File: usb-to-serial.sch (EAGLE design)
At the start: 3 parts, among them IC1 SX1308, J1 C10418, U1 CH340ESMD

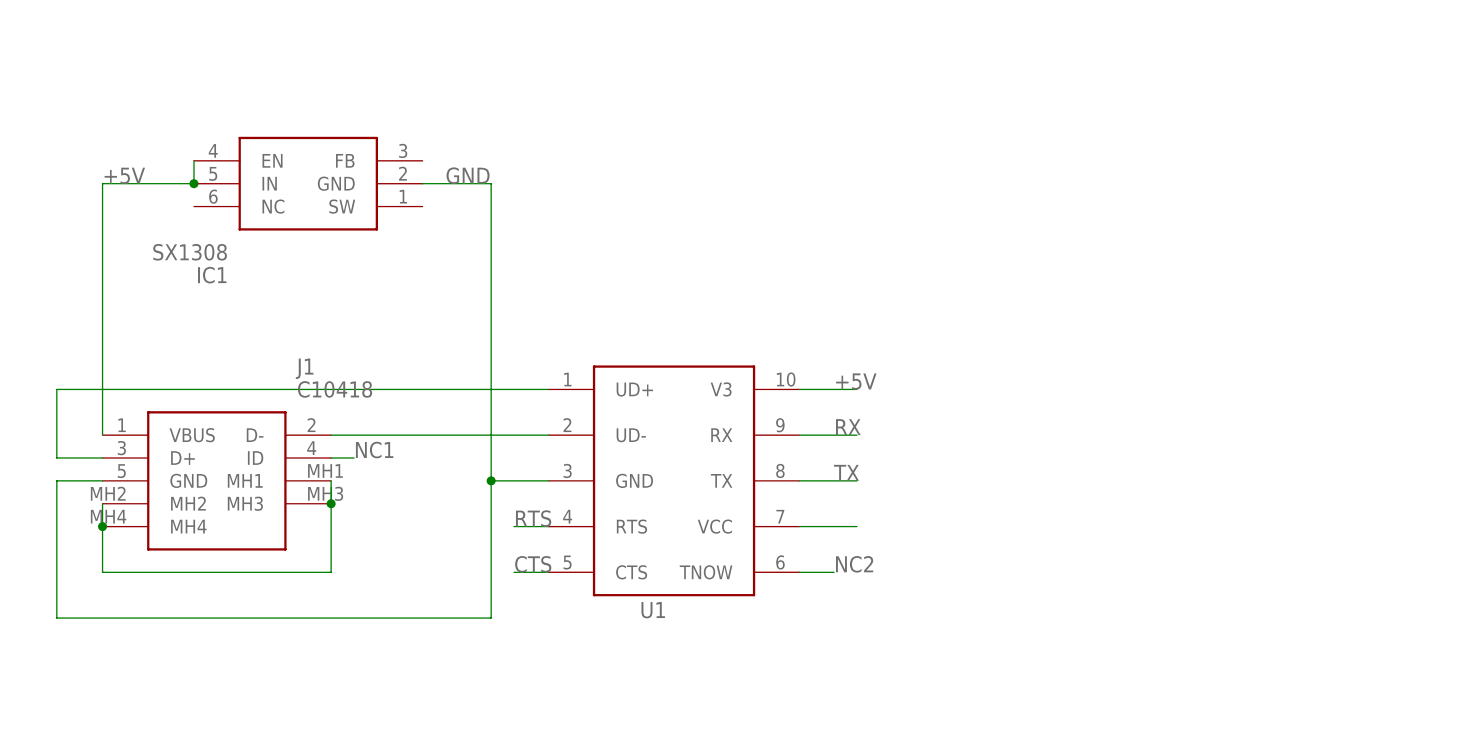
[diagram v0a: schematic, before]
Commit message: USB to Serial done
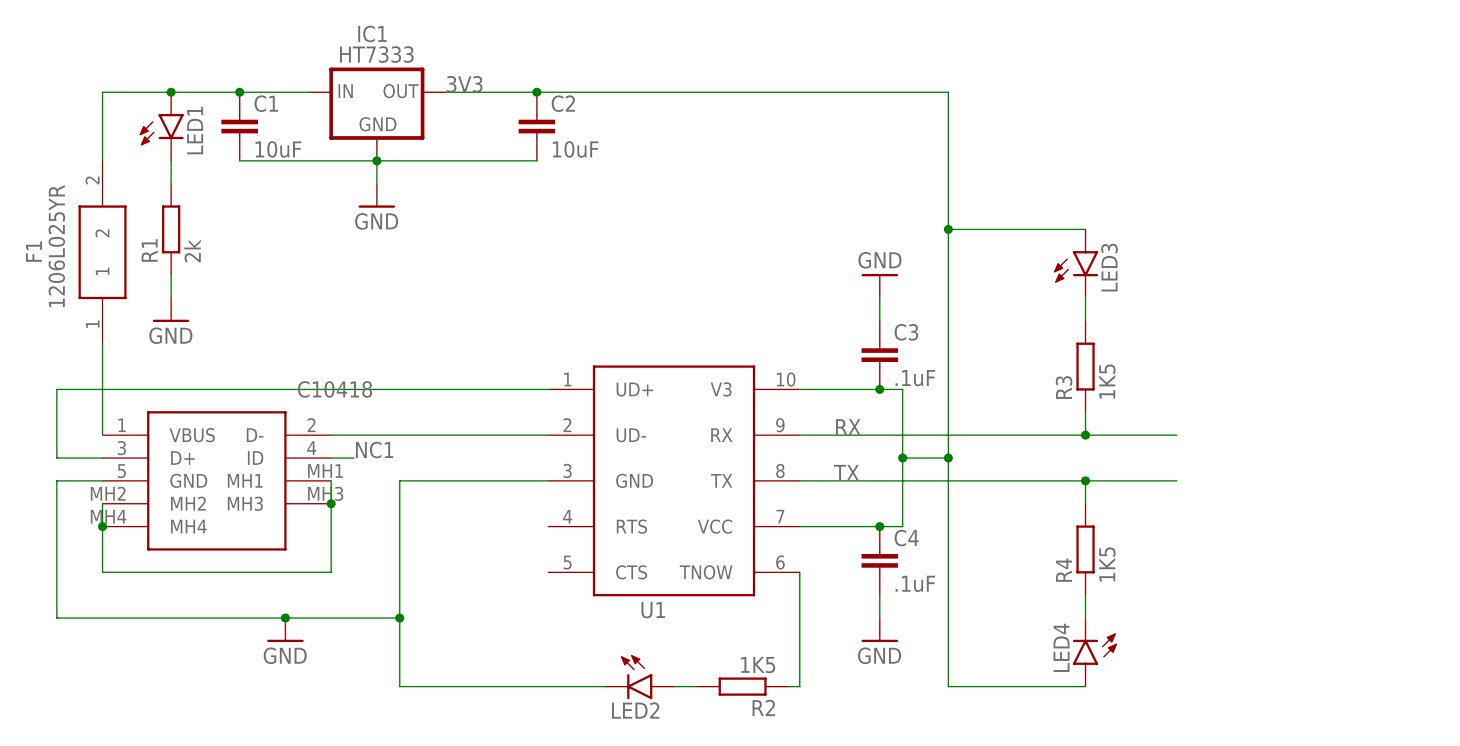
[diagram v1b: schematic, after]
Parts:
- added C1, C2: 10uF, rcl:C-EUC0805
- added C3, C4: .1uF, rcl:C-EUC0805
- added F1: 1206L025YR, water-lib:1206L025YR
- added LED1, LED2, LED3, LED4: (no value), led:LEDCHIP-LED0805
- added R1: 2k, rcl:R-EU_R0805
- added R2, R3, R4: 1K5, rcl:R-EU_R0805
- IC1: value SX1308 -> HT7333; device water-lib:SX1308 -> water-lib:HT7333
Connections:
- removed net CTS: U1.CTS
- removed net NC2: U1.TNOW
- removed net RTS: U1.RTS
- new net 3V3: C2.1, C3.2, C4.1, IC1.OUT, LED3.A, LED4.A, U1.V3, U1.VCC
- new net N$1: F1.1, J1.VBUS
- new net N$3: R2.1, U1.TNOW
- new net N$4: LED2.A, R2.2
- new net N$5: LED3.C, R3.2
- new net N$6: LED4.C, R4.1
- net +5V: now also C1.1, F1.2, LED1.A; no longer IC1.EN, J1.VBUS, U1.V3
- net GND: now also C1.2, C2.2, C3.1, C4.2, LED2.C, R1.1
- net N$2: now also LED1.C, R1.2; no longer U1.VCC
- net RX: now also R3.1
- net TX: now also R4.2

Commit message: Added pin header
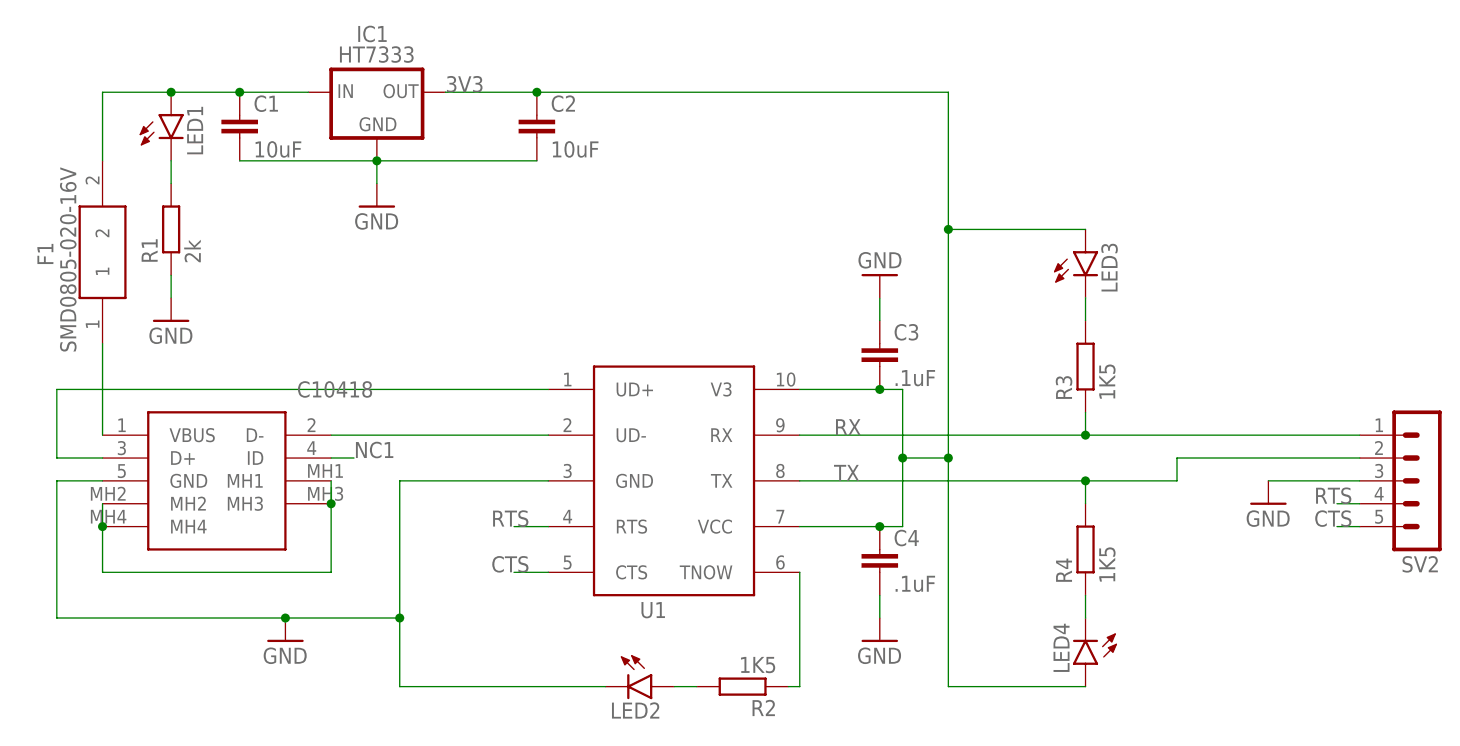
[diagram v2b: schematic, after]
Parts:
- added SV2: (no value), con-lstb:MA05-1
- F1: value 1206L025YR -> SMD0805-020-16V; device water-lib:1206L025YR -> water-lib:SMD0805-020-16V
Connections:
- new net CTS: SV2.5, U1.CTS
- new net RTS: SV2.4, U1.RTS
- net GND: now also SV2.3
- net RX: now also SV2.1
- net TX: now also SV2.2
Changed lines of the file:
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@@
 <part name="GND1" library="supply1" library_urn="urn:adsk.eagle:library:371" deviceset="GND" device=""/>
 <part name="GND2" library="supply1" library_urn="urn:adsk.eagle:library:371" deviceset="GND" device=""/>
-<part name="F1" library="water-lib" deviceset="1206L025YR" device=""/>
 <part name="LED1" library="led" library_urn="urn:adsk.eagle:library:259" deviceset="LED" device="CHIP-LED0805" package3d_urn="urn:adsk.eagle:package:15818/2"/>
 <part name="R1" library="rcl" library_urn="urn:adsk.eagle:library:334" deviceset="R-EU_" device="R0805" package3d_urn="urn:adsk.eagle:package:23553/2" value="2k"/>
@@
 <part name="R3" library="rcl" library_urn="urn:adsk.eagle:library:334" deviceset="R-EU_" device="R0805" package3d_urn="urn:adsk.eagle:package:23553/2" value="1K5"/>
 <part name="R4" library="rcl" library_urn="urn:adsk.eagle:library:334" deviceset="R-EU_" device="R0805" package3d_urn="urn:adsk.eagle:package:23553/2" value="1K5"/>
+<part name="GND6" library="supply1" library_urn="urn:adsk.eagle:library:371" deviceset="GND" device=""/>
+<part name="F1" library="water-lib" deviceset="SMD0805-020-16V" device=""/>
+<part name="SV2" library="con-lstb" library_urn="urn:adsk.eagle:library:162" deviceset="MA05-1" device="" package3d_urn="urn:adsk.eagle:package:8332/1"/>
 </parts>
 <sheets>
@@
 <attribute name="VALUE" x="22.86" y="45.72" size="1.778" layer="96"/>
 </instance>
-<instance part="F1" gate="G$1" x="5.08" y="81.28" smashed="yes" rot="R90">
-<attribute name="NAME" x="-2.54" y="90.17" size="1.778" layer="95" rot="R90" align="center-left"/>
-<attribute name="VALUE" x="0" y="85.09" size="1.778" layer="96" rot="R90" align="center-left"/>
-</instance>
 <instance part="LED1" gate="G$1" x="12.7" y="106.68" smashed="yes">
 <attribute name="NAME" x="16.256" y="102.108" size="1.778" layer="95" rot="R90"/>
@@
 <attribute name="NAME" x="112.8014" y="54.61" size="1.778" layer="95" rot="R90"/>
 <attribute name="VALUE" x="117.602" y="54.61" size="1.778" layer="96" rot="R90"/>
+</instance>
+<instance part="GND6" gate="1" x="134.62" y="63.5" smashed="yes">
+<attribute name="VALUE" x="132.08" y="60.96" size="1.778" layer="96"/>
+</instance>
+<instance part="F1" gate="G$1" x="5.08" y="81.28" smashed="yes" rot="R90">
+<attribute name="NAME" x="-1.27" y="89.916" size="1.778" layer="95" rot="R90" align="center-left"/>
+<attribute name="VALUE" x="1.27" y="80.264" size="1.778" layer="96" rot="R90" align="center-left"/>
+</instance>
+<instance part="SV2" gate="G$1" x="152.4" y="66.04" smashed="yes" rot="R180">
+<attribute name="VALUE" x="153.67" y="76.2" size="1.778" layer="96" rot="R180"/>
+<attribute name="NAME" x="153.67" y="57.658" size="1.778" layer="95" rot="R180"/>
 </instance>
 </instances>
@@
 <junction x="20.32" y="109.22"/>
 <pinref part="LED1" gate="G$1" pin="A"/>
-<pinref part="F1" gate="G$1" pin="2"/>
 <wire x1="5.08" y1="101.6" x2="5.08" y2="109.22" width="0.1524" layer="91"/>
 <wire x1="5.08" y1="109.22" x2="12.7" y2="109.22" width="0.1524" layer="91"/>
 <junction x="12.7" y="109.22"/>
+<pinref part="F1" gate="G$1" pin="2"/>
 </segment>
 </net>
@@
 <wire x1="91.44" y1="53.34" x2="91.44" y2="50.8" width="0.1524" layer="91"/>
 </segment>
+<segment>
+<pinref part="GND6" gate="1" pin="GND"/>
+<pinref part="SV2" gate="G$1" pin="3"/>
+<wire x1="134.62" y1="66.04" x2="144.78" y2="66.04" width="0.1524" layer="91"/>
+</segment>
 </net>
 <net name="D-" class="0">
@@
 <wire x1="114.3" y1="63.5" x2="114.3" y2="66.04" width="0.1524" layer="91"/>
 <junction x="114.3" y="66.04"/>
+<wire x1="124.46" y1="66.04" x2="124.46" y2="68.58" width="0.1524" layer="91"/>
+<pinref part="SV2" gate="G$1" pin="2"/>
+<wire x1="124.46" y1="68.58" x2="144.78" y2="68.58" width="0.1524" layer="91"/>
 </segment>
 </net>
@@
 <wire x1="82.55" y1="71.12" x2="114.3" y2="71.12" width="0.1524" layer="91"/>
 <pinref part="R3" gate="G$1" pin="1"/>
-<wire x1="114.3" y1="71.12" x2="124.46" y2="71.12" width="0.1524" layer="91"/>
 <wire x1="114.3" y1="73.66" x2="114.3" y2="71.12" width="0.1524" layer="91"/>
 <junction x="114.3" y="71.12"/>
+<wire x1="114.3" y1="71.12" x2="144.78" y2="71.12" width="0.1524" layer="91"/>
+<pinref part="SV2" gate="G$1" pin="1"/>
 </segment>
 </net>
@@
 </segment>
 </net>
+<net name="RTS" class="0">
+<segment>
+<pinref part="U1" gate="G$1" pin="RTS"/>
+<wire x1="54.61" y1="60.96" x2="50.8" y2="60.96" width="0.1524" layer="91"/>
+<label x="48.26" y="60.96" size="1.778" layer="95"/>
+</segment>
+<segment>
+<pinref part="SV2" gate="G$1" pin="4"/>
+<wire x1="144.78" y1="63.5" x2="142.24" y2="63.5" width="0.1524" layer="91"/>
+<label x="139.7" y="63.5" size="1.778" layer="95"/>
+</segment>
+</net>
+<net name="CTS" class="0">
+<segment>
+<pinref part="U1" gate="G$1" pin="CTS"/>
+<wire x1="54.61" y1="55.88" x2="50.8" y2="55.88" width="0.1524" layer="91"/>
+<label x="48.26" y="55.88" size="1.778" layer="95"/>
+</segment>
+<segment>
+<pinref part="SV2" gate="G$1" pin="5"/>
+<wire x1="144.78" y1="60.96" x2="142.24" y2="60.96" width="0.1524" layer="91"/>
+<label x="139.7" y="60.96" size="1.778" layer="95"/>
+</segment>
+</net>
